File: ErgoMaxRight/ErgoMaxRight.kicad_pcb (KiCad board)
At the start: 2 copper layers, 182.8 x 169.2 mm, 102 parts, among them J1 PJ-320A, K1 KEYSW, K10 KEYSW, K11 KEYSW, K12 KEYSW, K13 KEYSW, K14 KEYSW, K15 KEYSW, K16 KEYSW, K17 KEYSW, K18 KEYSW, K19 KEYSW, K2 KEYSW, K20 KEYSW, K21 KEYSW, K22 KEYSW, K23 KEYSW, K24 KEYSW, K25 KEYSW, K26 KEYSW, K27 KEYSW, K28 KEYSW, K29 KEYSW, K3 KEYSW, K30 KEYSW, K31 KEYSW, K32 KEYSW, K33 KEYSW, K34 KEYSW, K35 KEYSW, K36 KEYSW, K37 KEYSW, K38 KEYSW, K39 KEYSW, K4 KEYSW, K40 KEYSW, K41 KEYSW, K42 KEYSW, K43 KEYSW, K44 KEYSW, K5 KEYSW, K6 KEYSW, K7 KEYSW, K8 KEYSW, K9 KEYSW, U1 ProMicro

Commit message: add add values for main keys on PCB
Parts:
- K1: value KEYSW -> F12
- K10: value KEYSW -> 8 *
- K11: value KEYSW -> 7 &
- K12: value KEYSW -> 6 ^
- K15: value KEYSW -> P
- K16: value KEYSW -> O
- K17: value KEYSW -> I
- K18: value KEYSW -> U
- K19: value KEYSW -> Y
- K2: value KEYSW -> F11
- K22: value KEYSW -> ; :
- K23: value KEYSW -> L
- K24: value KEYSW -> K
- K25: value KEYSW -> J
- K26: value KEYSW -> H
- K3: value KEYSW -> F10
- K30: value KEYSW -> / ?
- K31: value KEYSW -> . >
- K32: value KEYSW -> , <
- K33: value KEYSW -> M
- K34: value KEYSW -> N
- K4: value KEYSW -> F9
- K5: value KEYSW -> F8
- K6: value KEYSW -> F7
- K8: value KEYSW -> 0 )
- K9: value KEYSW -> 9 (
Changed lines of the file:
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@@
       (effects (font (size 1.524 1.524) (thickness 0.3048)))
     )
-    (fp_text value KEYSW (at 0 7) (layer B.SilkS)
+    (fp_text value H (at 0 7) (layer B.SilkS)
       (effects (font (size 1.524 1.524) (thickness 0.3048)) (justify mirror))
     )
@@
       (effects (font (size 1.524 1.524) (thickness 0.3048)))
     )
-    (fp_text value KEYSW (at 0 7) (layer B.SilkS)
+    (fp_text value J (at 0 7) (layer B.SilkS)
       (effects (font (size 1.524 1.524) (thickness 0.3048)) (justify mirror))
     )
@@
       (effects (font (size 1.524 1.524) (thickness 0.3048)))
     )
-    (fp_text value KEYSW (at 0 7) (layer B.SilkS)
+    (fp_text value "/ ?" (at 0 7) (layer B.SilkS)
       (effects (font (size 1.524 1.524) (thickness 0.3048)) (justify mirror))
     )
@@
       (effects (font (size 1.524 1.524) (thickness 0.3048)))
     )
-    (fp_text value KEYSW (at 0 7) (layer B.SilkS)
+    (fp_text value ". >" (at 0 7) (layer B.SilkS)
       (effects (font (size 1.524 1.524) (thickness 0.3048)) (justify mirror))
     )
@@
       (effects (font (size 1.524 1.524) (thickness 0.3048)))
     )
-    (fp_text value KEYSW (at 0 7) (layer B.SilkS)
+    (fp_text value ", <" (at 0 7) (layer B.SilkS)
       (effects (font (size 1.524 1.524) (thickness 0.3048)) (justify mirror))
     )
@@
       (effects (font (size 1.524 1.524) (thickness 0.3048)))
     )
-    (fp_text value KEYSW (at 0 7) (layer B.SilkS)
+    (fp_text value M (at 0 7) (layer B.SilkS)
       (effects (font (size 1.524 1.524) (thickness 0.3048)) (justify mirror))
     )
@@
       (effects (font (size 1.524 1.524) (thickness 0.3048)))
     )
-    (fp_text value KEYSW (at 0 7) (layer B.SilkS)
+    (fp_text value N (at 0 7) (layer B.SilkS)
       (effects (font (size 1.524 1.524) (thickness 0.3048)) (justify mirror))
     )
@@
       (effects (font (size 1.524 1.524) (thickness 0.3048)))
     )
-    (fp_text value KEYSW (at 0 7) (layer B.SilkS)
+    (fp_text value F11 (at 0 7) (layer B.SilkS)
       (effects (font (size 1.524 1.524) (thickness 0.3048)) (justify mirror))
     )
@@
       (effects (font (size 1.524 1.524) (thickness 0.3048)))
     )
-    (fp_text value KEYSW (at 0 7) (layer B.SilkS)
+    (fp_text value F12 (at 0 7) (layer B.SilkS)
       (effects (font (size 1.524 1.524) (thickness 0.3048)) (justify mirror))
     )
@@
       (effects (font (size 1.524 1.524) (thickness 0.3048)))
     )
-    (fp_text value KEYSW (at 0 7) (layer B.SilkS)
+    (fp_text value F10 (at 0 7) (layer B.SilkS)
       (effects (font (size 1.524 1.524) (thickness 0.3048)) (justify mirror))
     )
@@
       (effects (font (size 1.524 1.524) (thickness 0.3048)))
     )
-    (fp_text value KEYSW (at 0 7) (layer B.SilkS)
+    (fp_text value F9 (at 0 7) (layer B.SilkS)
       (effects (font (size 1.524 1.524) (thickness 0.3048)) (justify mirror))
     )
@@
       (effects (font (size 1.524 1.524) (thickness 0.3048)))
     )
-    (fp_text value KEYSW (at 0 7) (layer B.SilkS)
+    (fp_text value F8 (at 0 7) (layer B.SilkS)
       (effects (font (size 1.524 1.524) (thickness 0.3048)) (justify mirror))
     )
@@
       (effects (font (size 1.524 1.524) (thickness 0.3048)))
     )
-    (fp_text value KEYSW (at 0 7) (layer B.SilkS)
+    (fp_text value F7 (at 0 7) (layer B.SilkS)
       (effects (font (size 1.524 1.524) (thickness 0.3048)) (justify mirror))
     )
@@
       (effects (font (size 1.524 1.524) (thickness 0.3048)))
     )
-    (fp_text value KEYSW (at 0 7) (layer B.SilkS)
+    (fp_text value "0 )" (at 0 7) (layer B.SilkS)
       (effects (font (size 1.524 1.524) (thickness 0.3048)) (justify mirror))
     )
@@
       (effects (font (size 1.524 1.524) (thickness 0.3048)))
     )
-    (fp_text value KEYSW (at 0 7) (layer B.SilkS)
+    (fp_text value "9 (" (at 0 7) (layer B.SilkS)
       (effects (font (size 1.524 1.524) (thickness 0.3048)) (justify mirror))
     )
@@
       (effects (font (size 1.524 1.524) (thickness 0.3048)))
     )
-    (fp_text value KEYSW (at 0 7) (layer B.SilkS)
+    (fp_text value "8 *" (at 0 7) (layer B.SilkS)
       (effects (font (size 1.524 1.524) (thickness 0.3048)) (justify mirror))
     )
@@
       (effects (font (size 1.524 1.524) (thickness 0.3048)))
     )
-    (fp_text value KEYSW (at 0 7) (layer B.SilkS)
+    (fp_text value "7 &" (at 0 7) (layer B.SilkS)
       (effects (font (size 1.524 1.524) (thickness 0.3048)) (justify mirror))
     )
@@
       (effects (font (size 1.524 1.524) (thickness 0.3048)))
     )
-    (fp_text value KEYSW (at 0 7) (layer B.SilkS)
+    (fp_text value "6 ^" (at 0 7) (layer B.SilkS)
       (effects (font (size 1.524 1.524) (thickness 0.3048)) (justify mirror))
     )
@@
       (effects (font (size 1.524 1.524) (thickness 0.3048)))
     )
-    (fp_text value KEYSW (at 0 7) (layer B.SilkS)
+    (fp_text value K (at 0 7) (layer B.SilkS)
       (effects (font (size 1.524 1.524) (thickness 0.3048)) (justify mirror))
     )
@@
       (effects (font (size 1.524 1.524) (thickness 0.3048)))
     )
-    (fp_text value KEYSW (at 0 7) (layer B.SilkS)
+    (fp_text value P (at 0 7) (layer B.SilkS)
       (effects (font (size 1.524 1.524) (thickness 0.3048)) (justify mirror))
     )
@@
       (effects (font (size 1.524 1.524) (thickness 0.3048)))
     )
-    (fp_text value KEYSW (at 0 7) (layer B.SilkS)
+    (fp_text value O (at 0 7) (layer B.SilkS)
       (effects (font (size 1.524 1.524) (thickness 0.3048)) (justify mirror))
     )
@@
       (effects (font (size 1.524 1.524) (thickness 0.3048)))
     )
-    (fp_text value KEYSW (at 0 7) (layer B.SilkS)
+    (fp_text value I (at 0 7) (layer B.SilkS)
       (effects (font (size 1.524 1.524) (thickness 0.3048)) (justify mirror))
     )
@@
       (effects (font (size 1.524 1.524) (thickness 0.3048)))
     )
-    (fp_text value KEYSW (at 0 7) (layer B.SilkS)
+    (fp_text value U (at 0 7) (layer B.SilkS)
       (effects (font (size 1.524 1.524) (thickness 0.3048)) (justify mirror))
     )
@@
       (effects (font (size 1.524 1.524) (thickness 0.3048)))
     )
-    (fp_text value KEYSW (at 0 7) (layer B.SilkS)
+    (fp_text value Y (at 0 7) (layer B.SilkS)
       (effects (font (size 1.524 1.524) (thickness 0.3048)) (justify mirror))
     )
@@
       (effects (font (size 1.524 1.524) (thickness 0.3048)))
     )
-    (fp_text value KEYSW (at 0 7) (layer B.SilkS)
+    (fp_text value "; :" (at 0 7) (layer B.SilkS)
       (effects (font (size 1.524 1.524) (thickness 0.3048)) (justify mirror))
     )
@@
       (effects (font (size 1.524 1.524) (thickness 0.3048)))
     )
-    (fp_text value KEYSW (at 0 7) (layer B.SilkS)
-      (effects (font (size 1.524 1.524) (thickness 0.3048)) (justify mirror))
-    )
+    (fp_text value L (at 0 7) (layer B.SilkS)
+      (effects (font (size 1.524 1.524) (thickness 0.3048)) (justify mirror))
+    )

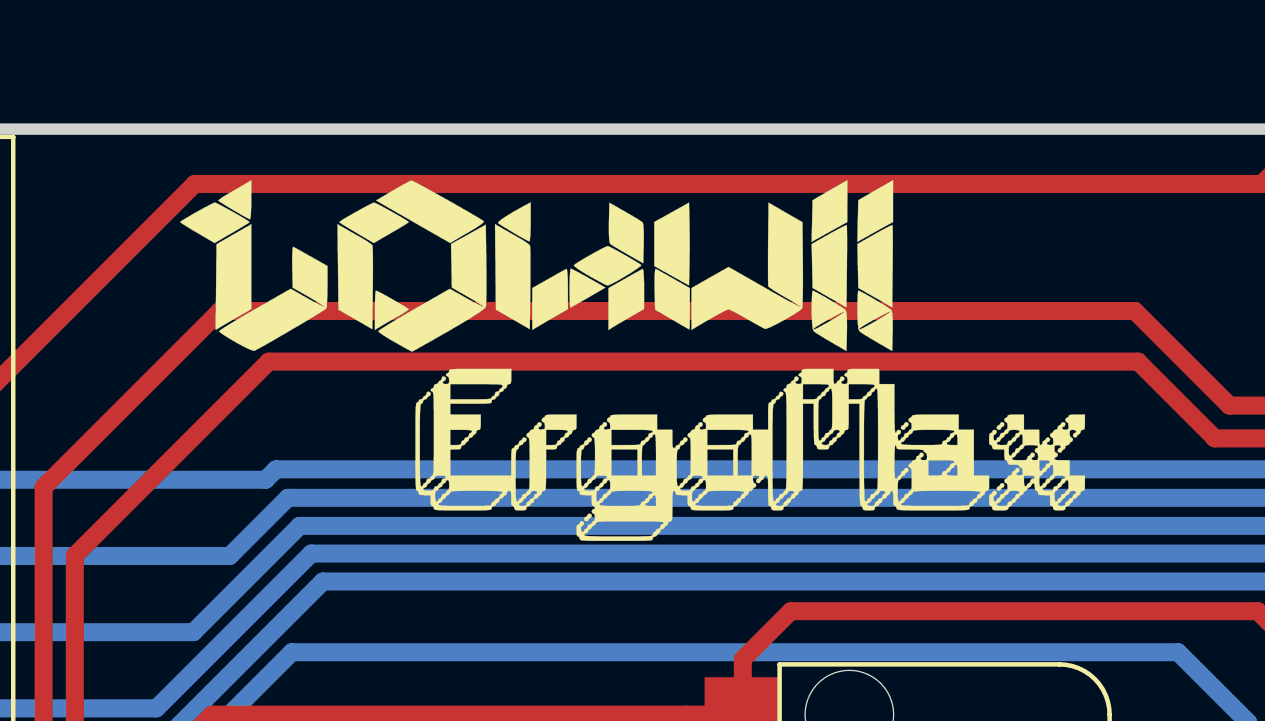
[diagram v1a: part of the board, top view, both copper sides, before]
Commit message: move logos to front side of left and right PCB, add left/right writings
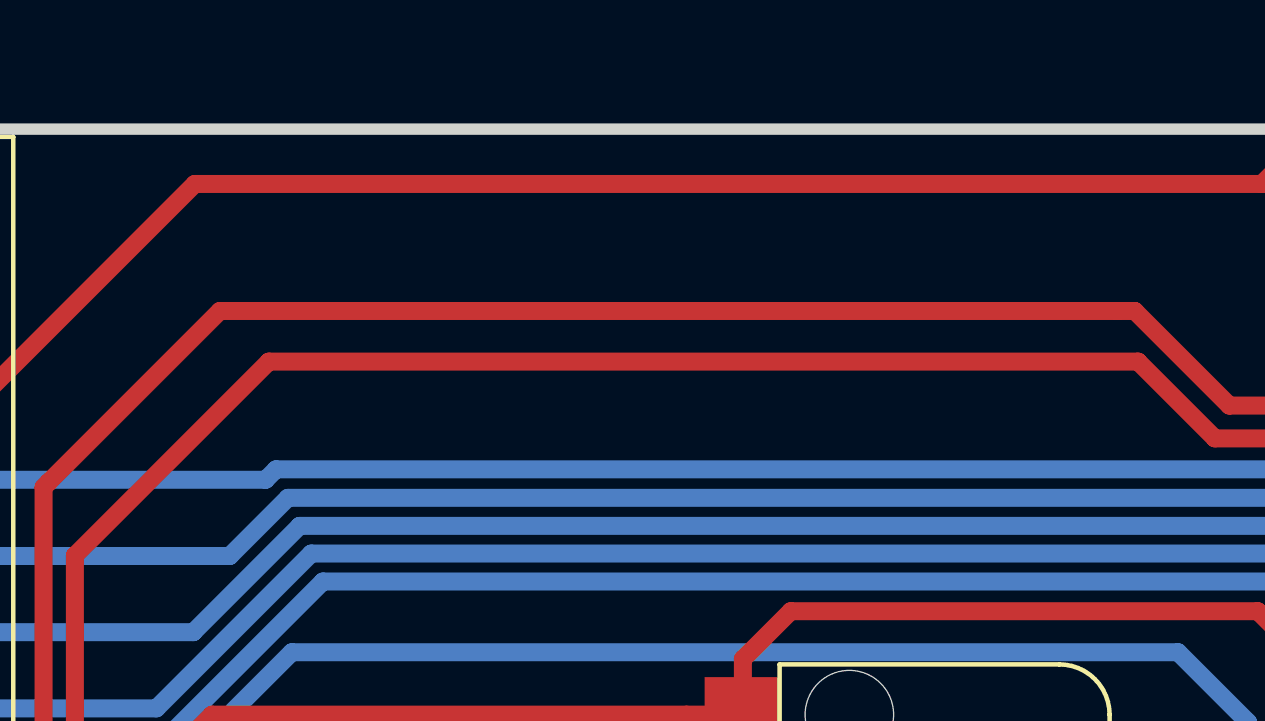
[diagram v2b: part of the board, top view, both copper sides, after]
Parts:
- added Lg3: Logo, ErgoMax:RightSideText, F.Cu at (208.8, 45.3)
- Lg1, Lg2: moved to B.Cu
- turned Lg1 to 180 degrees
- turned Lg2 to 180 degrees
